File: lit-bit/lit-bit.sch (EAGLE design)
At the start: 15 parts, among them U1 S-1317A33-M5T1U4, U2 32U4, U3 MCP73831T, Y1 8MHz

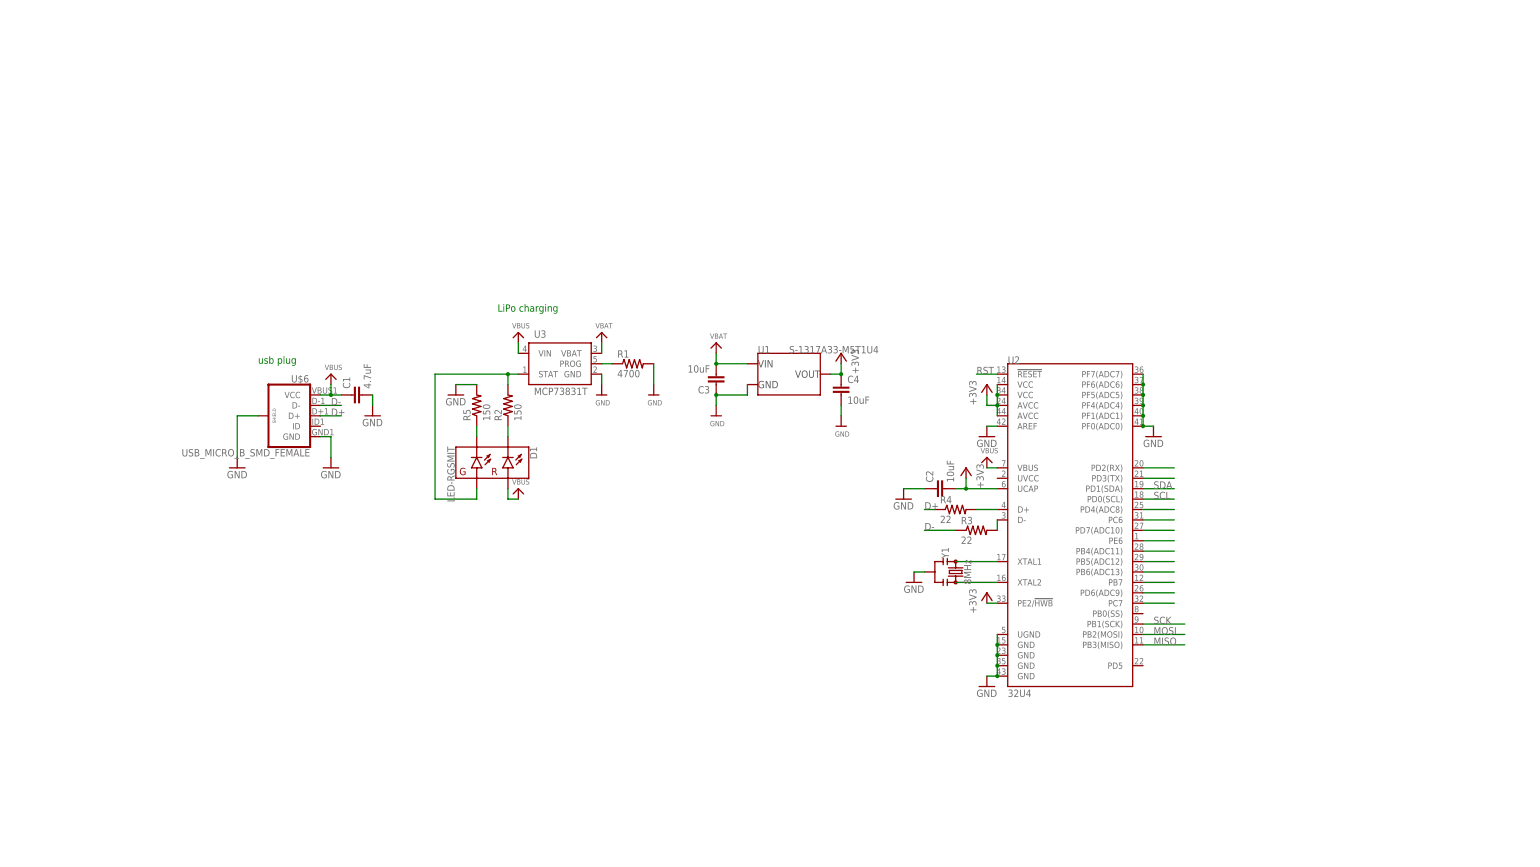
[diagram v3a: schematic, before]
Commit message: Added all the major components to sch working on BLE antenna
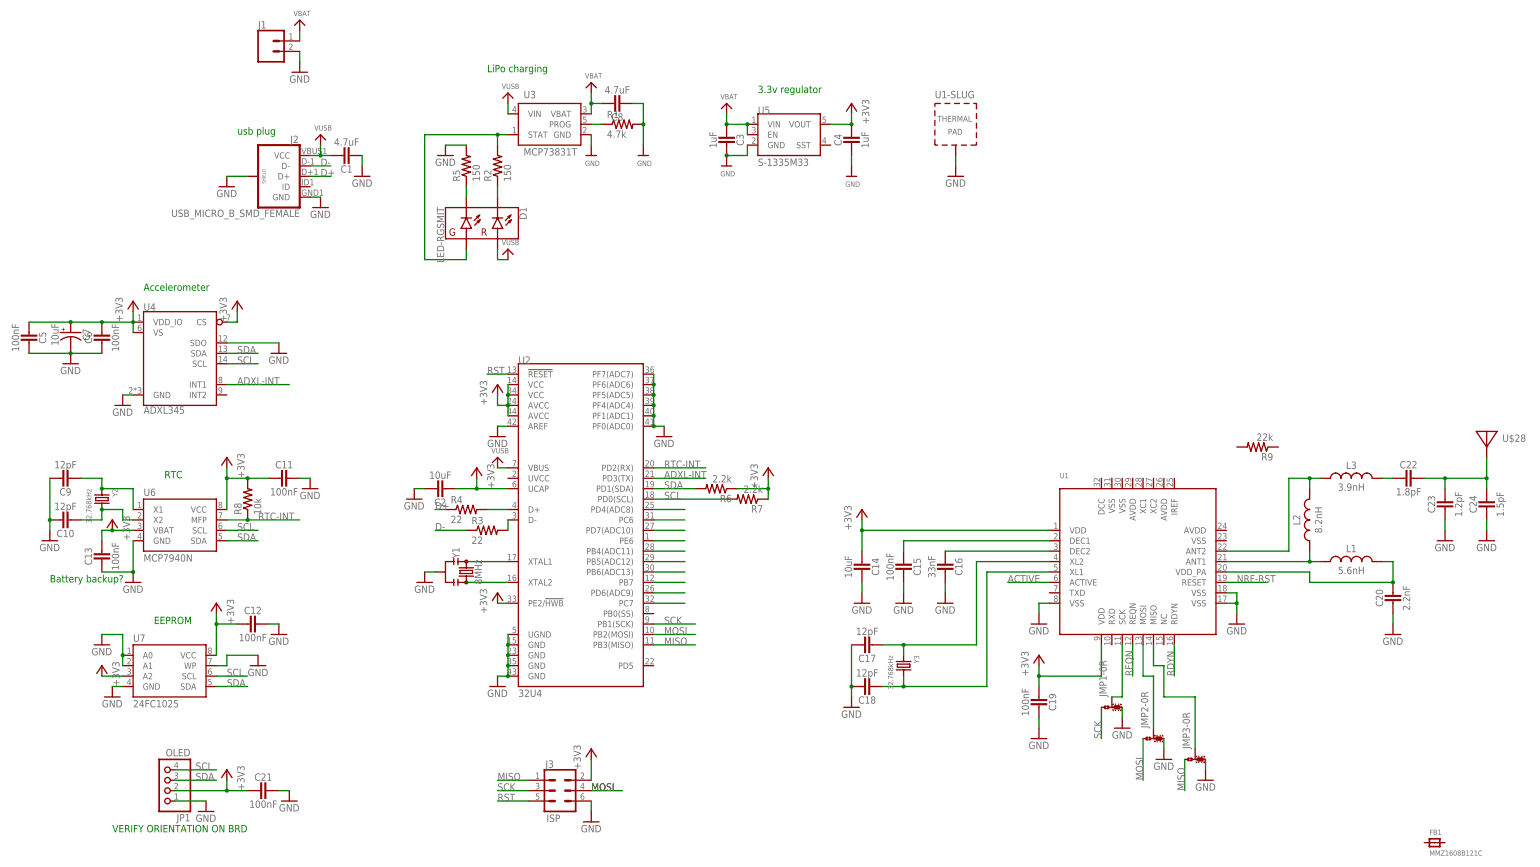
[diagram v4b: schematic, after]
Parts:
- removed U$6: USB_MICRO_B_SMD_FEMALE, SCADA_CUSTOM_LIBRARY:USB_MICRO_B_SMD_FEMALE
- added C10, C17, C18, C9: 12pF, SCADA_CUSTOM_LIBRARY:CAP_NONPOL
- added C11, C12, C13, C15, C19, C21, C5, C6: 100nF, SCADA_CUSTOM_LIBRARY:CAP_NONPOL0603
- added C14: 10uF, SCADA_CUSTOM_LIBRARY:CAP_NONPOL0603
- added C16: 33nF, SCADA_CUSTOM_LIBRARY:CAP_NONPOL0603
- added C20: 2.2nF, SCADA_CUSTOM_LIBRARY:CAP_NONPOL0603
- added C22: 1.8pF, SCADA_CUSTOM_LIBRARY:CAP_NONPOL0603
- added C23: 1.2pF, SCADA_CUSTOM_LIBRARY:CAP_NONPOL0603
- added C24: 1.5pF, SCADA_CUSTOM_LIBRARY:CAP_NONPOL0603
- added C7: 10uF, SCADA_CUSTOM_LIBRARY:CAP_POL
- added C8: 4.7uF, SCADA_CUSTOM_LIBRARY:CAP_NONPOL0603
- added FB1: MMZ1608B121C, microbuilder:FERRITE0805
- added J1: (no value), SparkFun-Connectors:CONN_02-JST-2MM-SMT
- added J2: USB_MICRO_B_SMD_FEMALE, SCADA_CUSTOM_LIBRARY:USB_MICRO_B_SMD_FEMALE
- added J3: ISP, SCADA_CUSTOM_LIBRARY:CONN_03X2SMT
- added JMP1, JMP2, JMP3: 0R-JUMPA, jump-0r-smd:0R-JUMPA
- added JP1: OLED, pinhead:PINHD-1X4
- added L1: 5.6nH, SCADA_CUSTOM_LIBRARY:INDUCTOR0603
- added L2: 8.2nH, SCADA_CUSTOM_LIBRARY:INDUCTOR0603
- added L3: 3.9nH, SCADA_CUSTOM_LIBRARY:INDUCTOR0603
- added R6, R7: 2.2k, SCADA_CUSTOM_LIBRARY:RES-0603
- added R8: 10k, SCADA_CUSTOM_LIBRARY:RES-0603
- added R9: 22k, SCADA_CUSTOM_LIBRARY:RES-0603
- added U$28: (no value), microbuilder:ANTENNA_PCBNRF8001_1.6MM
- added U4: ADXL345, SCADA_CUSTOM_LIBRARY:ADXL345
- added U5: S-1335M33, SCADA_CUSTOM_LIBRARY:S-1335M33
- added U6: MCP7940N, SCADA_CUSTOM_LIBRARY:MCP7940N
- added U7: 24FC1025, SCADA_CUSTOM_LIBRARY:24FC1025
- added Y2, Y3: 32.768kHz, SCADA_CUSTOM_LIBRARY:CRYSTAL8X3.8SMT
- C1, C2: device SCADA_CUSTOM_LIBRARY:CAP_NONPOL_0805 -> SCADA_CUSTOM_LIBRARY:CAP_NONPOL0603
- C3, C4: value 10uF -> 1uF; device SCADA_CUSTOM_LIBRARY:CAP_NONPOL_0805 -> SCADA_CUSTOM_LIBRARY:CAP_NONPOL0603
- R1: value 4700 -> 4.7k; device SCADA_CUSTOM_LIBRARY:RES-0805 -> SCADA_CUSTOM_LIBRARY:RES-0603
- R2, R3, R4, R5: device SCADA_CUSTOM_LIBRARY:RES-0805 -> SCADA_CUSTOM_LIBRARY:RES-0603
- U1: value S-1317A33-M5T1U4 -> (none); device SCADA_CUSTOM_LIBRARY:S-1317A33-M5T1U4 -> SCADA_CUSTOM_LIBRARY:NRF8001
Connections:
- removed net VBUS: C1.1, D1.RA, U$6.VCC, U2.VBUS, U3.VIN
- new net ACTIVE: U1A.ACTIVE
- new net ADXL-INT: U2.PD3(TX), U4.INT1
- new net N$20: C9.2, U6.X1, Y2.1
- new net N$21: C10.2, U6.X2, Y2.2
- new net N$22: C16.2, U1A.DEC2
- new net N$23: C18.2, U1A.XL1, Y3.2
- new net N$24: C20.1, L1.2, U1A.VDD_PA
- new net N$25: L1.1, L2.1, U1A.ANT1
- new net N$26: J3.2
- new net N$27: JMP1-0R.2, U1A.SCK
- new net N$28: L2.2, L3.1, U1A.ANT2
- new net N$29: JMP2-0R.2, U1A.MOSI
- new net N$31: C22.2, L3.2
- new net N$32: C22.1, C23.1, C24.1, U$28.P$1
- new net N$34: JMP3-0R.2, U1A.MISO
- new net NRF-RST: U1A.RESET
- new net RDYN: U1A.RDYN
- new net REQN: U1A.REQN
- new net RTC-INT: R8.1, U2.PD2(RX), U6.MFP
- new net VUSB: D1.RA, U2.VBUS
- net +3V3: now also C11.2, C12.2, C13.1, C14.2, C19.2, C21.2, C5.2, C6.1, C7.+, JP1.2, R6.1, R7.1, R8.2, U1A.VDD@1, U1A.VDD@2, U4.CS, U4.VDD_IO, U4.VS, U5.VOUT, U6.VBAT, U6.VCC, U7.A2, U7.VCC; no longer U1.VOUT
- net D+: now also J2.D+; no longer U$6.D+
- net D-: now also J2.D-; no longer U$6.D-
- net GND: now also C10.1, C11.1, C12.1, C13.2, C14.1, C15.1, C16.1, C17.1, C18.1, C19.1, C20.2, C21.1, C23.2, C24.2, C5.1, C6.2, C7.-, C8.2, C9.1, J1.1, J2.GND, J2.SHIELD, J3.6, JMP1-0R.3, JMP2-0R.3, JMP3-0R.3, JP1.1, U1-SLUG.TP, U1A.VSS@1, U1A.VSS@2, U1A.VSS@3, U4.GND, U4.SDO, U5.GND, U6.GND, U7.A0, U7.A1, U7.GND, U7.WP; no longer U$6.GND, U$6.SHIELD, U1.GND
- net MISO: now also J3.1, JMP3-0R.1
- net MOSI: now also J3.4, JMP2-0R.1
- net N$15: now also C17.2, U1A.XL2, Y3.1; no longer U2.PD3(TX)
- net N$16: now also C15.2, U1A.DEC1; no longer U2.PD2(RX)
- net RST: now also J3.5
- net SCK: now also J3.3, JMP1-0R.1
- net SCL: now also JP1.4, R7.2, U4.SCL, U6.SCL, U7.SCL
- net SDA: now also JP1.3, R6.2, U4.SDA, U6.SDA, U7.SDA
- net VBAT: now also C1.1, C8.1, J1.2, J2.VCC, U3.VIN, U5.EN, U5.VIN; no longer U1.VIN
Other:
- note added: "3.3v regulator"
- note added: "Accelerometer"
- note added: "Battery backup?"
- note added: "EEPROM"
- note added: "RTC"
- note added: "VERIFY ORIENTATION ON BRD"
- moved on the sheet: C1, C2, C3, C4, D1, R1, R2, R3, R4, R5, U2, U3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

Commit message: finished the schematic starting on the brd now
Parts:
- removed JMP1, JMP2, JMP3: 0R-JUMPA, jump-0r-smd:0R-JUMPA
- added 3V3, SCL, SDA, VBAT: LSP10, solpad:LSP10
- added C25, C26: 100nF, SCADA_CUSTOM_LIBRARY:CAP_NONPOL0603
- added C27: 1uF, SCADA_CUSTOM_LIBRARY:CAP_NONPOL0603
- added C28, C29: 16pF, SCADA_CUSTOM_LIBRARY:CAP_NONPOL0603
- added J4, J5: (no value), SparkFun-Connectors:CONN_02
- added L4: 15nH, SCADA_CUSTOM_LIBRARY:INDUCTOR0603
- added L5: 10uH, SCADA_CUSTOM_LIBRARY:INDUCTOR0603
- added SJ1, SJ2, SJ3: (no value), microbuilder:SOLDERJUMPERWAVE
- added Y4: 16MHz, SCADA_CUSTOM_LIBRARY:CRYSTALTHIN
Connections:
- new net 3V3: FB1.P$1, J5.1
- new net AVDD: C25.2, C26.1, C27.1, FB1.P$2, L4.2, U1A.AVDD@1, U1A.AVDD@2, U1A.AVDD@3
- new net N$30: R9.2, U1A.IREF
- new net N$33: C28.2, U1A.XC1, Y4.2
- new net N$35: L4.1, L5.2
- new net N$36: L5.1, U1A.DCC
- new net N$37: C29.2, U1A.XC2, Y4.1
- new net N$41: C3.2, J4.2, U5.EN, U5.VIN
- net +3V3: now also 3V3.MP, J5.2
- net GND: now also C25.1, C26.2, C27.2, C28.1, C29.1, R9.1, U1A.VSS@4, U1A.VSS@5, U1A.VSS@6; no longer JMP1-0R.3, JMP2-0R.3, JMP3-0R.3
- net MISO: now also SJ3.1; no longer JMP3-0R.1
- net MOSI: now also SJ2.1; no longer JMP2-0R.1
- net N$27: now also SJ1.2; no longer JMP1-0R.2
- net N$29: now also SJ2.2; no longer JMP2-0R.2
- net N$34: now also SJ3.2; no longer JMP3-0R.2
- net SCK: now also SJ1.1; no longer JMP1-0R.1
- net SCL: now also SCL.MP
- net SDA: now also SDA.MP
- net VBAT: now also J4.1, VBAT.MP; no longer C3.2, U5.EN, U5.VIN
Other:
- note added: "Analog Supply Filtering"
- moved on the sheet: FB1, R6, R7, R9

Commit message: working through pcb placement
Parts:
- removed C13: 100nF, SCADA_CUSTOM_LIBRARY:CAP_NONPOL0603
- removed SJ1, SJ2, SJ3: (no value), microbuilder:SOLDERJUMPERWAVE
- added JP2: sck, SparkFun-Jumpers:JUMPER-SMT_2_NO_SILK
- added JP3: mosi, SparkFun-Jumpers:JUMPER-SMT_2_NO_SILK
- added JP4: miso, SparkFun-Jumpers:JUMPER-SMT_2_NO_SILK
- added R10: 10k, SCADA_CUSTOM_LIBRARY:RES-0603
- added SPR: LSP10, solpad:LSP10
- C10, C17, C18, C9: device SCADA_CUSTOM_LIBRARY:CAP_NONPOL -> SCADA_CUSTOM_LIBRARY:CAP_NONPOL0603
- D1: value LED-RGSMIT -> LEDs
- U3: value MCP73831T -> 73831
- U5: value S-1335M33 -> S-1335
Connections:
- removed net N$10: U2.PB7
- removed net N$11: U2.PB6(ADC13)
- removed net N$12: U2.PB5(ADC12)
- removed net N$13: U2.PB4(ADC11)
- removed net N$14: U2.PD7(ADC10)
- removed net N$17: U2.PD6(ADC9)
- removed net N$18: U2.PC7
- removed net N$19: U2.PD4(ADC8)
- removed net N$8: U2.PE6
- net +3V3: now also JP1.3; no longer C13.1, JP1.2
- net 3V3: now also R10.2
- net ACTIVE: now also R10.1, U2.PB7
- net GND: now also JP1.4; no longer C13.2, JP1.1
- net MISO: now also JP4.1; no longer SJ3.1
- net MOSI: now also JP3.1; no longer SJ2.1
- net N$27: now also JP2.2; no longer SJ1.2
- net N$29: now also JP3.2; no longer SJ2.2
- net N$34: now also JP4.2; no longer SJ3.2
- net N$9: now also SPR.MP
- net NRF-RST: now also U2.PD6(ADC9)
- net RDYN: now also U2.PE6
- net REQN: now also U2.PB5(ADC12)
- net SCK: now also JP2.1; no longer SJ1.1
- net SCL: now also JP1.1; no longer JP1.4
- net SDA: now also JP1.2; no longer JP1.3
- net VBAT: no longer C1.1, J2.VCC, U3.VIN
- net VUSB: now also C1.1, J2.VCC, U3.VIN
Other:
- moved on the sheet: C21

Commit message: finally laid out the board
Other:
- moved on the sheet: C10, C11, C12, C14, C15, C16, C17, C18, C19, C20, C22, C23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

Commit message: acktually done with layout now, got board dimensions
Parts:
- JP1: device pinhead:PINHD-1X4 -> microbuilder:HEADER-1X4ROUND
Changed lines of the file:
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@@
 <part name="U$6" library="SCADA_CUSTOM_LIBRARY" deviceset="VUSB" device=""/>
 <part name="R8" library="SCADA_CUSTOM_LIBRARY" deviceset="RES-0603" device="" value="10k"/>
-<part name="JP1" library="pinhead" library_urn="urn:adsk.eagle:library:325" deviceset="PINHD-1X4" device="" package3d_urn="urn:adsk.eagle:package:22407/2" value="OLED"/>
+<part name="JP1" library="microbuilder" deviceset="HEADER-1X4" device="ROUND" value="OLED"/>
 <part name="+3V13" library="SCADA_CUSTOM_LIBRARY" deviceset="3V3" device=""/>
 <part name="+3V14" library="SCADA_CUSTOM_LIBRARY" deviceset="3V3" device=""/>
